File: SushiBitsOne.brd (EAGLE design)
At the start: 68.6 x 53.3 mm, 58 parts, among them IC1 CH340B, IC2 LM3671-3.3DBV, IC3 TPS562200DBV, J1 ARDUINO_R3, J2 DC-005, Q1 2N7002, Q2 MMBT2222A, U1 STM32F103CBT6-LQFP48, X1 32768Hz, X2 8MHz, X3 JTAG

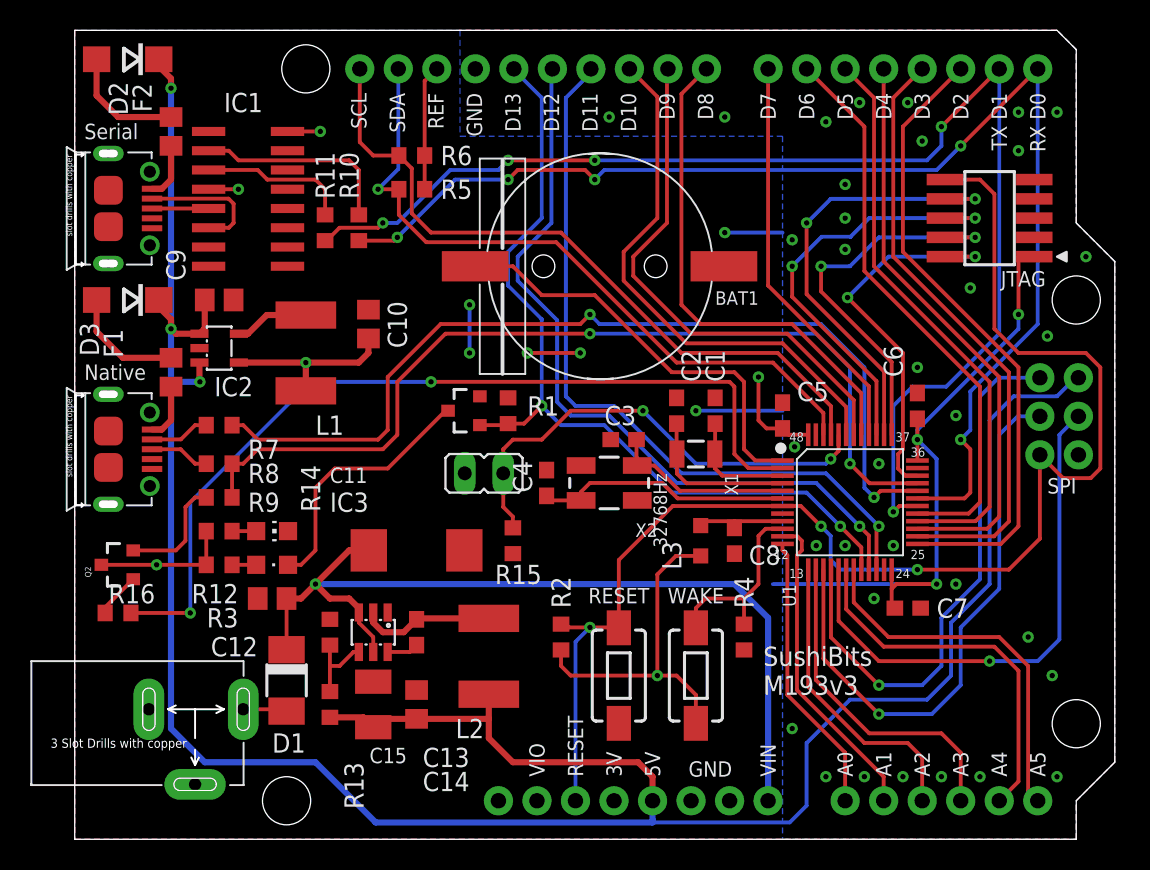
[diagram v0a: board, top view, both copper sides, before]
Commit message: Relayout the board to accomodate component changes.
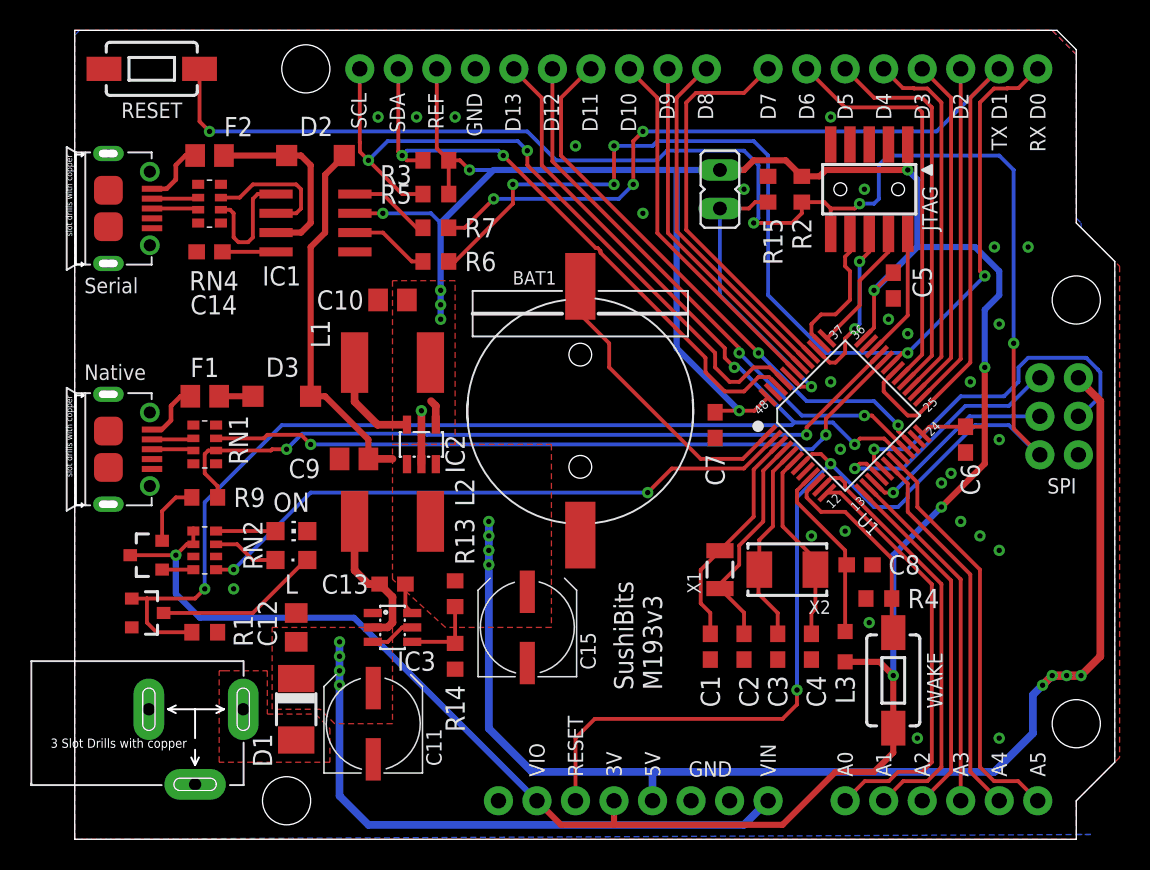
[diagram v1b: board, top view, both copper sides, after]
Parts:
- removed R10, R11: 10k, rcl:R0603
- removed R12: 1k, rcl:R0603
- removed R16: 4.7k, rcl:R0603
- removed R8: 22, rcl:R0603
- added RN1, RN4: 22, resistor-dil:EXB38V
- added RN2: 510, resistor-dil:EXB38V
- C11: value 47u -> 100u; device rcl:SMC_D -> rcl:UD-6,3X7,7_NICHICON
- C14: value 10u -> 1u; device rcl:C0805 -> rcl:C0603
- C15: value 47u -> 220u; device rcl:SMC_B -> rcl:UD-6,3X5,8_NICHICON
- D2, D3: device diode:DO214AC -> diode:SOD123
- IC1: value CH340B -> HT42B534; device WCH:SO16 -> HT42B534:SO8
- R3: value 330 -> 4.7k
- R6: value 4.7k -> 510
- R7: value 22 -> 510
- X2: device SparkFun-Clocks:CRYSTAL-SMD-5X3.2-4PAD -> SparkFun-Clocks:CRYSTAL-SMD-5X3.2-2PAD
- moved S1 50.5 mm to (5.08, 50.8), turned to 0 degrees
- moved R2 33.5 mm to (47.9, 42.9), turned to 90 degrees
- moved C14 32.8 mm to (8.89, 38.7), turned to 180 degrees
- moved R3 30.3 mm to (23.8, 44.8), turned to 0 degrees
- moved R15 28.6 mm to (45.7, 42.9), turned to 270 degrees
- moved Q1 24.8 mm to (4.76, 14.9), turned to 270 degrees
- moved R1 24.8 mm to (8.57, 13.7), turned to 180 degrees
- moved JP1 24.4 mm to (42.5, 42.9), turned to 180 degrees
- moved C4 20.5 mm to (48.6, 12.7), turned to 270 degrees
- moved R7 19.3 mm to (23.8, 40.3)
- moved C7 17.5 mm to (42.2, 27.3), turned to 270 degrees
- moved C3 17.0 mm to (46.4, 12.7), turned to 270 degrees
- moved C2 16.2 mm to (44.1, 12.7), turned to 270 degrees
- moved C1 15.6 mm to (41.9, 12.7), turned to 270 degrees
- moved IC2 14.8 mm to (22.9, 26.0), turned to 0 degrees
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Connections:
- new net N$21: C14.1, IC1.8
- new net N$22: RN4.3, USB2.3
- new net N$23: RN4.2, USB2.2
- net +3V3: now also IC1.3, RN2.1, RN2.2; no longer IC1.16, IC1.4, R12.2, R6.2
- net +5V: no longer C14.1
- net D14: now also RN2.5; no longer R16.2
- net HSEIN: now also X2.P$1; no longer X2.1
- net HSEOUT: now also X2.P$2; no longer X2.3
- net N$1: now also RN1.2; no longer R7.1
- net N$16: now also IC1.7
- net N$19: now also RN2.4; no longer R16.1
- net N$2: now also RN1.3; no longer R8.1
- net N$3: now also RN4.7; no longer USB2.2
- net N$4: now also RN4.6; no longer USB2.3
- net N$5: now also R6.1; no longer R10.1
- net N$6: now also IC1.4, R7.1; no longer IC1.3, R11.1
- net N$7: now also RN2.8; no longer R12.1
- net N$9: now also RN2.7; no longer R3.1
- net RXD: now also R6.2; no longer R10.2
- net SCL: now also R5.1; no longer R6.1
- net SDA: now also R3.1; no longer R5.1
- net TXD: now also R7.2; no longer R11.2
- net UD+: now also RN1.6; no longer R8.2
- net UD-: now also RN1.7; no longer R7.2
- net VBUS: now also F2.1, USB2.1; no longer F1.1, USB1.1
- net VBUS2: now also F1.1, USB1.1; no longer F2.1, USB2.1
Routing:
- net +3V3: track 111.0 -> 210.7 mm, vias 11 -> 12
- net +5V: track 168.4 -> 110.0 mm, vias 3 -> 8
- net RESET#: track 91.0 -> 145.9 mm, vias 3 -> 6
- net D13: track 55.8 -> 96.1 mm, vias 2 -> 3
- net SCK: track 38.0 -> 13.3 mm
- net JTDI: track 29.8 -> 9.38 mm, vias 2 -> 0
- net MISO: track 36.9 -> 16.8 mm
- net D2: track 42.0 -> 22.7 mm
- net D14: track 58.5 -> 40.3 mm
- net JTDO: track 28.8 -> 11.0 mm
- net JTCK: track 26.1 -> 8.56 mm, vias 2 -> 0
- net JTMS: track 26.0 -> 8.51 mm, vias 2 -> 0
- net D3: track 40.2 -> 23.0 mm
- net VIN: track 59.7 -> 42.9 mm, vias 1 -> 4
- net D4: track 38.4 -> 24.3 mm
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- added copper zone on layer 1, net +3V3
- added copper zone on layer 1, net +5V
- added copper zone on layer 1, net N$11
- added copper zone on layer 1, net VIN
- removed copper zone on layer 16, net +3V3
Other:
- board text added: "L"
- board text added: "ON"

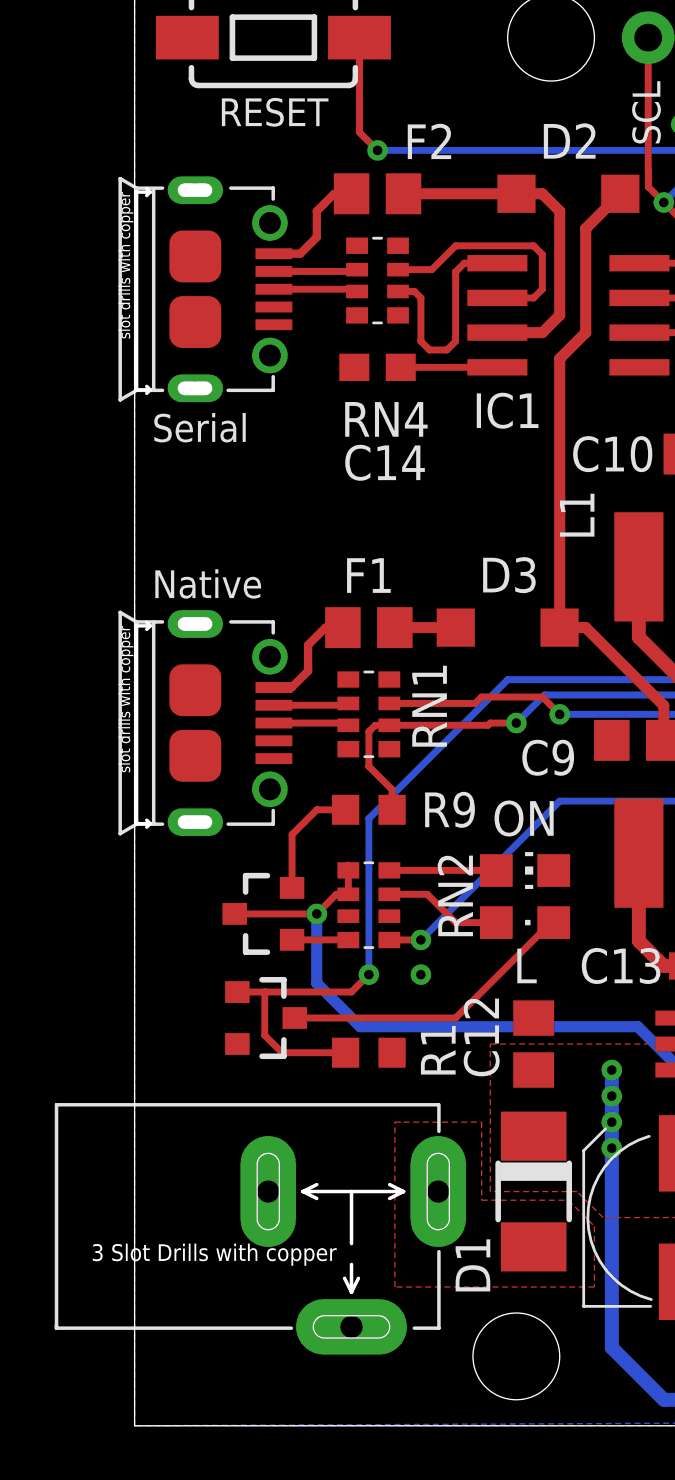
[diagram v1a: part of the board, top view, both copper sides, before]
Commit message: Change up some footprints.
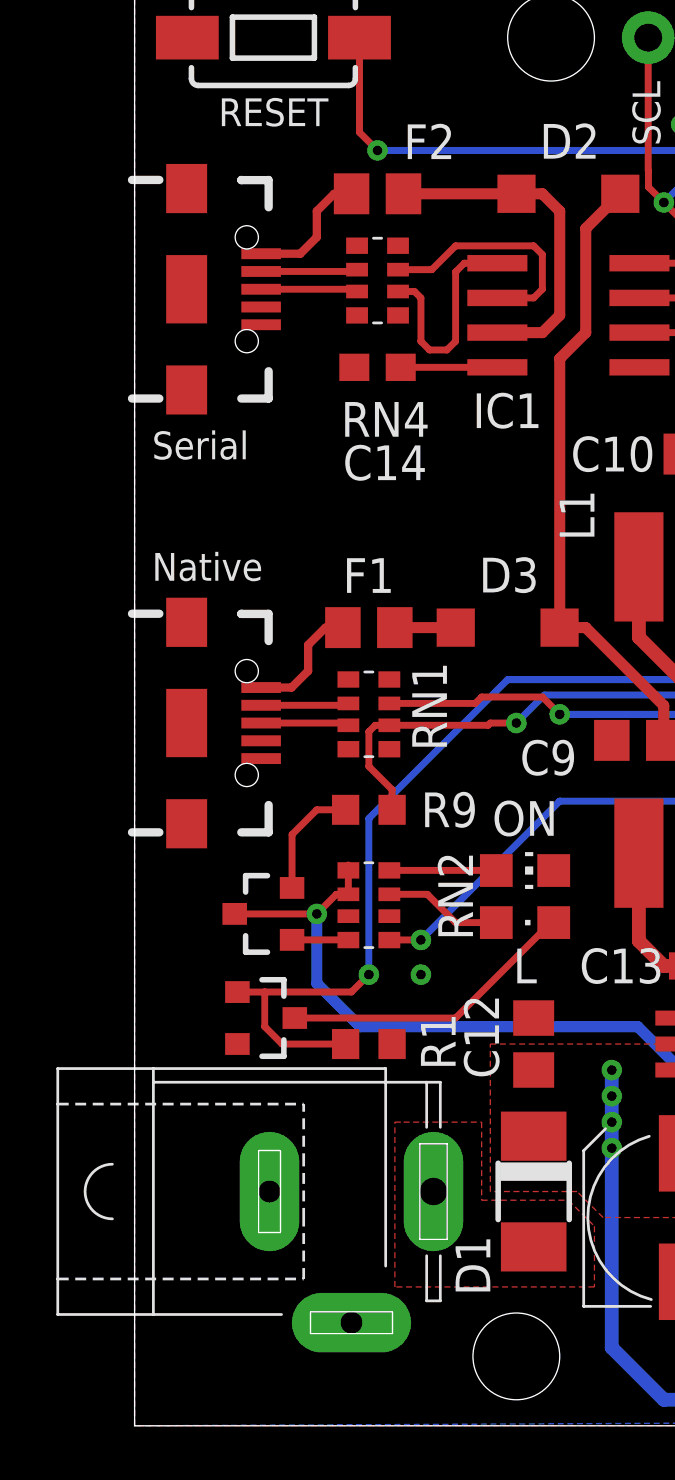
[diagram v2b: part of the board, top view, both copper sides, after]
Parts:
- removed USB1, USB2: ZX62-B-5PA, Seeed-OPL-Connector:MICRO-USB5+6P-SMD-0.65-AB
- added J3, J4: (no value), SparkFun-Connectors:USB-B-MICRO-SMD
- J2: value DC-005 -> (none); device Seeed-OPL-Connector:DCJ3P-14.2X11.0X9.0MM -> con-jack:SPC4077
- moved R1 0.32 mm to (8.57, 14.0)
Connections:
- removed net VBUS: F2.1, USB2.1
- new net N$24: F2.1, J3.VBUS
- net GND: now also J2.1, J2.2, J3.GND, J3.SHIELD1, J3.SHIELD2, J3.SHIELD3, J4.GND, J4.SHIELD1, J4.SHIELD2, J4.SHIELD3; no longer J2.-1, J2.-2, USB1.5, USB1.P1, USB1.P2, USB1.P3, USB1.P4, USB1.P5, USB1.P6, USB2.5, USB2.P1, USB2.P2, USB2.P3, USB2.P4, USB2.P5, USB2.P6
- net N$1: now also J4.D-; no longer USB1.2
- net N$11: now also J2.3; no longer J2.+
- net N$2: now also J4.D+; no longer USB1.3
- net N$22: now also J3.D+; no longer USB2.3
- net N$23: now also J3.D-; no longer USB2.2
- net VBUS2: now also J4.VBUS; no longer USB1.1
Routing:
- net N$24: track 0.00 -> 4.78 mm
- net VBUS: track 4.31 -> 0.00 mm
- net N$22: track 3.08 -> 3.66 mm
- net N$2: track 2.76 -> 3.34 mm
- net N$23: track 3.07 -> 3.63 mm
- net N$1: track 2.75 -> 3.32 mm

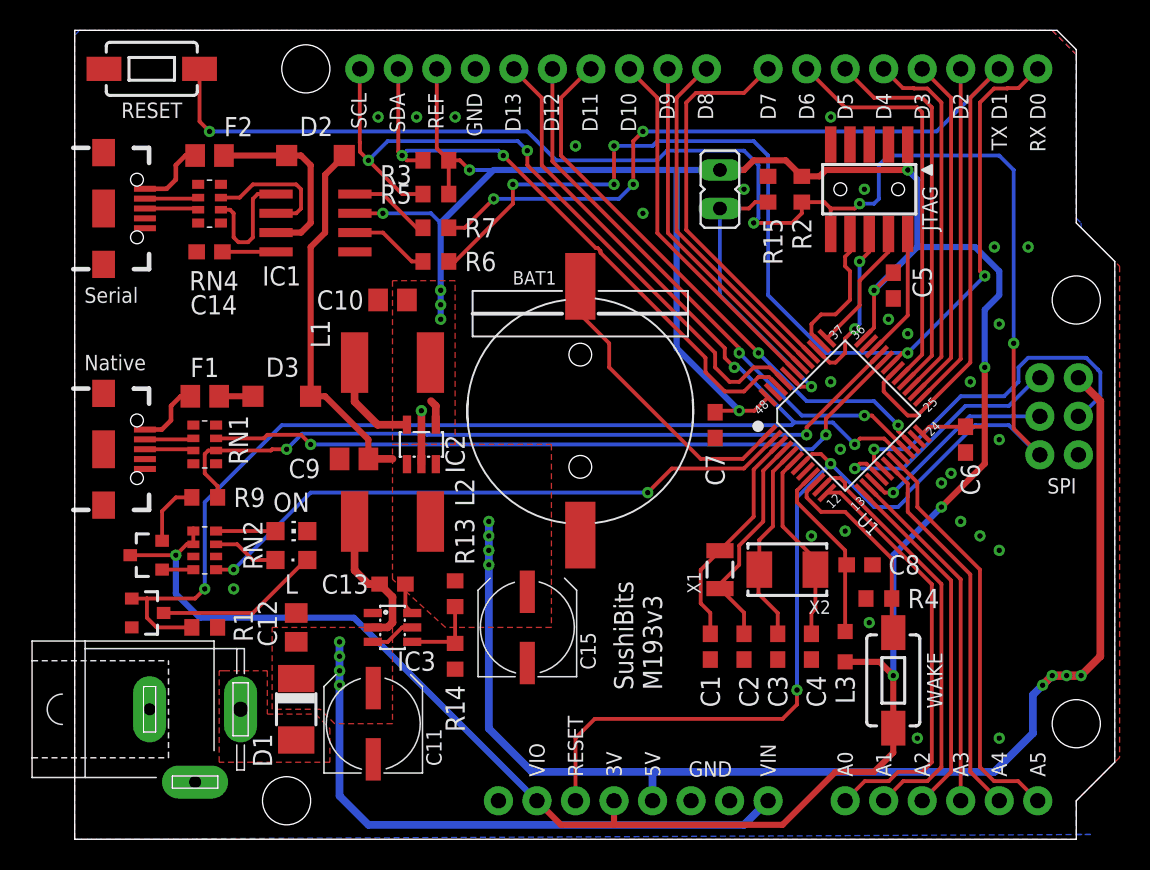
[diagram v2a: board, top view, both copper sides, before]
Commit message: Some manufacturability and cleanup work
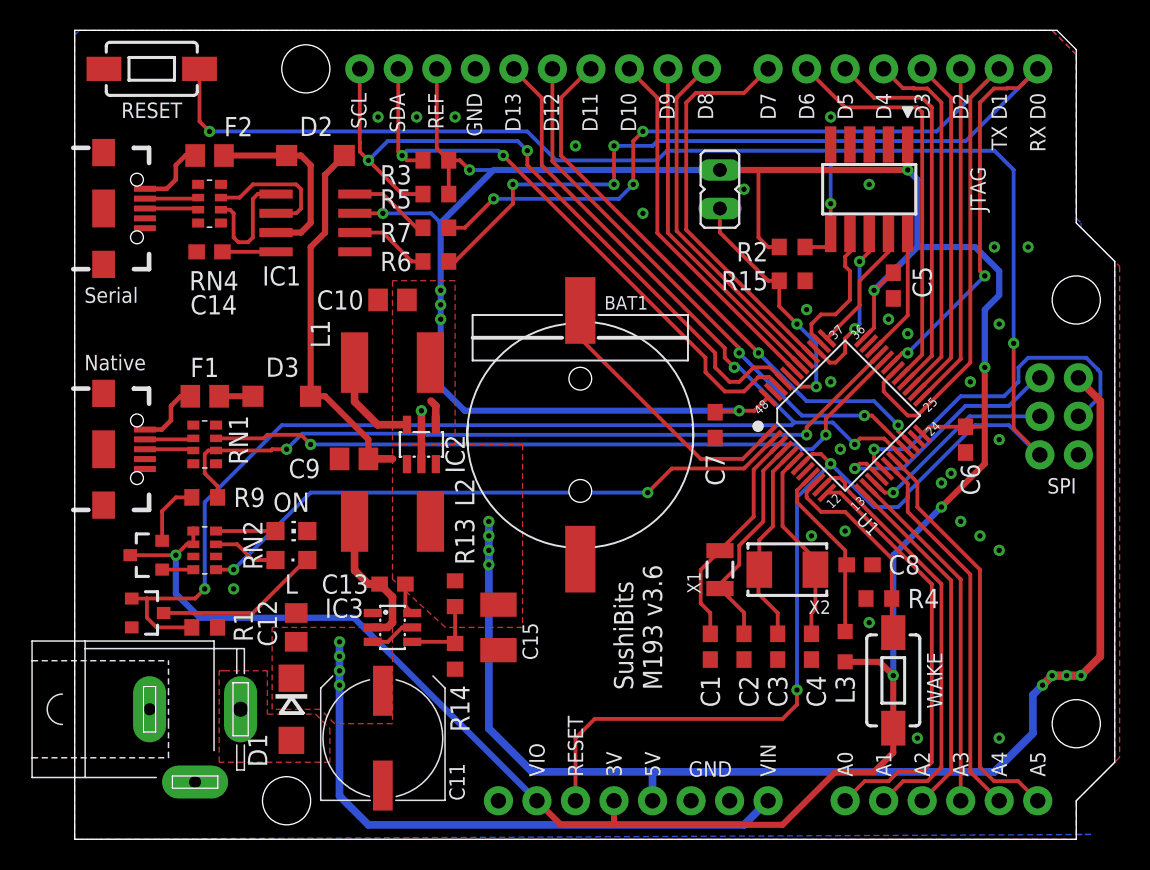
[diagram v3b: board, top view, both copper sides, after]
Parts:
- C11: device rcl:UD-6,3X7,7_NICHICON -> rcl:UD-8X10_NICHICON
- C15: device rcl:UD-6,3X5,8_NICHICON -> rcl:SMC_B
- D1: device diode:DO-214AC -> diode:DO214AC
- moved R15 6.24 mm to (47.3, 36.8), turned to 180 degrees
- moved R2 3.86 mm to (47.3, 39.1), turned to 180 degrees
- moved C15 1.90 mm to (27.9, 14.0), turned to 270 degrees
- moved BAT1 1.59 mm to (33.3, 26.7)
- moved C11 1.14 mm to (20.3, 6.67)
- moved D1 0.32 mm to (14.3, 8.57)
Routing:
- net +3V3: track 210.7 -> 223.1 mm
- net RESET#: track 145.9 -> 143.6 mm, vias 6 -> 5
- net N$12: track 19.3 -> 17.3 mm, vias 1 -> 2
- net VBAT: track 19.8 -> 18.2 mm
- net RXD: track 71.9 -> 71.3 mm
- net GND: vias 29 -> 30
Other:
- board text added: "SushiBits M193 v3.6"
- board text removed: "SushiBits M193v3"

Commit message: Squeezed the onboard debugger back in.
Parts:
- added C16: 22p, rcl:C0603
- added C17: 100n, rcl:C0603
- added IC4: (no value), v-reg:SOT23
- added LED3: Amber, led:CHIP-LED0805
- added LED4: Green, led:CHIP-LED0805
- added R8: 10k, rcl:R0603
- added RN3, RN5: 510, resistor-dil:EXB38V
- added X4: 1365-10, con-leotronics:1365-10
- added Y1: 8M, SparkFun-Clocks:CRYSTAL-SMD-5X3.2-2PAD
- C14: value 1u -> 22p
- IC1: value HT42B534 -> STM32F042F6P6; device HT42B534:SO8 -> HeadphoneBT:TSSOP20
- moved C14 7.94 mm to (16.5, 36.5), turned to 90 degrees
- moved D2 6.55 mm to (10.8, 49.2), turned to 270 degrees
- moved IC1 1.59 mm to (14.9, 41.9)
- moved C10 0.95 mm to (21.9, 35.6)
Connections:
- new net N$25: IC1.20, X4.4
- new net N$26: IC1.19, X4.2
- new net N$27: C17.1, IC1.16, IC1.5, IC4.2, RN5.6, RN5.7, X4.1
- new net N$28: C14.1, IC1.2, Y1.P$1
- new net N$29: C16.1, IC1.3, Y1.P$2
- new net N$30: IC1.11, RN3.1
- new net N$31: IC1.12, RN3.2
- new net N$32: IC1.13, RN3.3
- new net N$33: IC1.14, RN3.4
- new net N$34: IC1.1, R8.2
- new net N$35: IC1.6, LED3.C
- new net N$36: IC1.7, LED4.C
- new net N$37: LED4.A, RN5.2
- new net N$38: LED3.A, RN5.3
- net +3V3: no longer IC1.3
- net GND: now also C16.2, C17.2, IC1.15, IC4.1, R8.1, X4.3, X4.5, X4.9; no longer IC1.1
- net JTCK: now also RN3.7
- net JTDI: now also RN3.6
- net JTDO: now also RN3.5
- net JTMS: now also RN3.8
- net N$16: now also IC4.3; no longer IC1.7
- net N$21: now also IC1.4, X4.10; no longer C14.1, IC1.8
- net N$3: now also IC1.17; no longer IC1.6
- net N$4: now also IC1.18; no longer IC1.5
- net N$5: now also IC1.8; no longer IC1.2
- net N$6: now also IC1.9; no longer IC1.4
- net RESET#: now also IC1.10
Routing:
- net N$27: track 0.00 -> 76.9 mm, vias 0 -> 3
- net N$36: track 0.00 -> 40.2 mm, vias 0 -> 2
- net N$35: track 0.00 -> 38.1 mm, vias 0 -> 2
- net N$32: track 0.00 -> 30.7 mm, vias 0 -> 2
- net N$30: track 0.00 -> 30.6 mm, vias 0 -> 2
- net N$31: track 0.00 -> 29.8 mm, vias 0 -> 2
- net N$33: track 0.00 -> 29.0 mm, vias 0 -> 2
- net JTMS: track 8.51 -> 36.5 mm, vias 0 -> 2
- net JTCK: track 8.56 -> 34.5 mm, vias 0 -> 2
- net JTDO: track 11.0 -> 33.9 mm, vias 2 -> 3
- net JTDI: track 9.38 -> 30.9 mm, vias 0 -> 2
- net N$21: track 3.54 -> 20.7 mm, vias 0 -> 2
- net +5V: track 110.0 -> 127.1 mm, vias 8 -> 10
- net N$29: track 0.00 -> 14.7 mm
- net N$28: track 0.00 -> 10.3 mm
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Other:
- board text added: "SushiBits M193v6"
- board text removed: "SushiBits M193 v3.6"
